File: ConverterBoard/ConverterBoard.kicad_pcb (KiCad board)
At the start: 2 copper layers, 60 x 55 mm, 51 parts, among them J1 PWR_IN, J2 PWR_OUT1, J3 PWR_OUT2, J4 PWR_OUT3, U1 RT6285, U2 RT6285, U3 RT6285

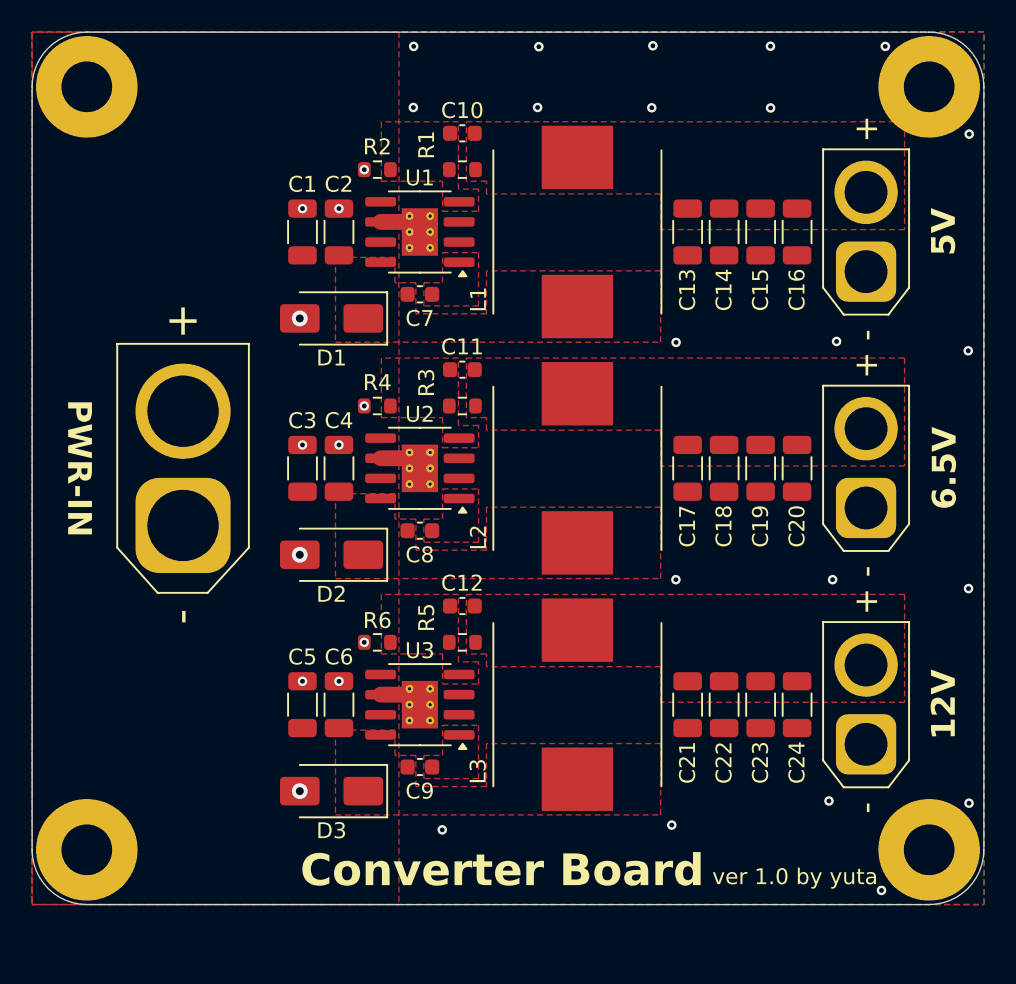
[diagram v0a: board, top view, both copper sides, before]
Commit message: Converter Board ver1.1
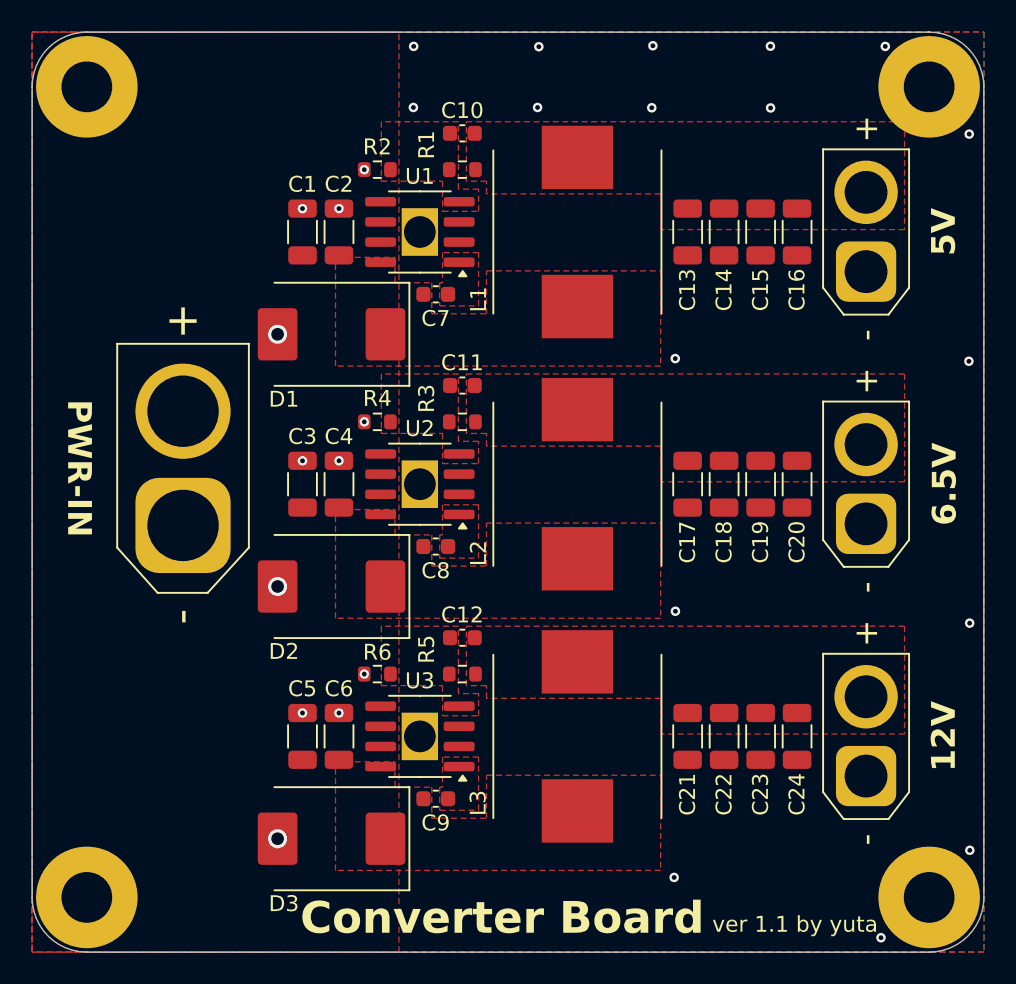
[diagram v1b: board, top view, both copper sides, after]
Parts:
- D1, D2, D3: footprint Diode_SMD:D_SMA -> Diode_SMD:D_SMC
- U1, U2, U3: footprint Package_SO:SOIC-8-1EP_3.9x4.9mm_P1.27mm_EP2.29x3mm_ThermalVias -> Anan-Robo_Footprint_Library:SOIC-8-1EP_3.9x4.9mm_P1.27mm_EP2.29x3mm_Handsoldering
- moved D3 3.00 mm to (122.8, 125.0)
- moved H6 3.00 mm to (121.0, 128.5)
- moved H3 3.00 mm to (107.3, 128.7)
- moved H4 3.00 mm to (160.4, 128.7)
- moved C9 2.24 mm to (129.3, 122.5)
- moved C12 2.00 mm to (131.0, 112.3)
- moved C21 2.00 mm to (145.2, 118.5)
- moved C22 2.00 mm to (147.5, 118.5)
- moved C23 2.00 mm to (149.8, 118.5)
- moved C24 2.00 mm to (152.1, 118.5)
- moved C5 2.00 mm to (120.9, 118.5)
- moved C6 2.00 mm to (123.2, 118.5)
- moved D2 2.00 mm to (122.8, 109.1)
- moved J4 2.00 mm to (156.4, 121.0)
- moved L3 2.00 mm to (138.2, 118.5)
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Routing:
- net GNDA: track 8.21 -> 0.90 mm, vias 33 -> 29
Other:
- board size 60 x 55 mm -> 60 x 58 mm
- board text added: "ver 1.1: 2025-06-12"
- board text removed: "ver 1.0: 2025-05-31"

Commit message: [Converter Board] : 基板上の日付を修正
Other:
- board text added: "ver 1.1: 2025-06-17"
- board text removed: "ver 1.1: 2025-06-12"
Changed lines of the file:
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@@
 		)
 	)
-	(gr_text "ver 1.1: 2025-06-12"
+	(gr_text "ver 1.1: 2025-06-17"
 		(at 136.5 76 180)
 		(layer "B.SilkS")
@@
 			(justify left mirror)
 		)
-		(render_cache "ver 1.1: 2025-06-12" 180
+		(render_cache "ver 1.1: 2025-06-17" 180
 			(polygon
 				(pts
@@
 			(polygon
 				(pts
-					(xy 154.829351 75.6791) (xy 154.834175 75.705449) (xy 154.849061 75.729878) (xy 154.960509 75.847921)
-					(xy 155.104783 76.002893) (xy 155.186775 76.092212) (xy 155.242536 76.154494) (xy 155.294926 76.220073)
-					(xy 155.33105 76.279131) (xy 155.351349 76.335355) (xy 155.358893 76.388967) (xy 155.352951 76.43921)
-					(xy 155.336193 76.479714) (xy 155.308848 76.512725) (xy 155.272983 76.536879) (xy 155.227215 76.552271)
-					(xy 155.16875 76.557861) (xy 155.098146 76.551505) (xy 155.022791 76.53163) (xy 154.940799 76.500415)
-					(xy 154.855582 76.456159) (xy 154.855582 76.682425) (xy 154.949005 76.71276) (xy 155.026088 76.731591)
-					(xy 155.110738 76.744001) (xy 155.190073 76.748004) (xy 155.27697 76.742566) (xy 155.357281 76.726682)
-					(xy 155.431396 76.698421) (xy 155.493349 76.657806) (xy 155.53984 76.610532) (xy 155.574462 76.553758)
-					(xy 155.595581 76.488456) (xy 155.603185 76.406993) (xy 155.597531 76.341872) (xy 155.580251 76.275834)
-					(xy 155.545188 76.205559) (xy 155.496646 76.134857) (xy 155.412163 76.041361) (xy 155.258876 75.883971)
-					(xy 155.164647 75.795457) (xy 155.10808 75.752812) (xy 155.065436 75.71515) (xy 155.606482 75.71515)
-					(xy 155.606482 75.502) (xy 154.829351 75.502)
-				)
-			)
+					(xy 155.355669 76.511919) (xy 154.845764 76.511919) (xy 154.845764 76.72507) (xy 155.619598 76.72507)
+					(xy 155.619598 76.554564) (xy 155.203189 75.502) (xy 154.957212 75.502)
+				)
+			)

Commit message: Converter Board ver1.2
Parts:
- added D4: BATT, LED_SMD:LED_0603_1608Metric, F.Cu at (107.0, 105.7)
- added D5: 5V, LED_SMD:LED_0603_1608Metric, F.Cu at (161.3, 85.6)
- added D6: 6.5V, LED_SMD:LED_0603_1608Metric, F.Cu at (161.3, 100.6)
- added D7: 12V, LED_SMD:LED_0603_1608Metric, F.Cu at (161.3, 116.8)
- added R10: 500, Resistor_SMD:R_0603_1608Metric, F.Cu at (161.3, 115.1)
- added R7: 1.5k, Resistor_SMD:R_0603_1608Metric, F.Cu at (107.0, 107.5)
- added R8: 240, Resistor_SMD:R_0603_1608Metric, F.Cu at (161.3, 83.8)
- added R9: 390, Resistor_SMD:R_0603_1608Metric, F.Cu at (161.3, 98.9)
- L3: value 33u -> 22u
- R6: value 11.3k -> 18k
- moved H7 7.50 mm to (142.0, 109.8)
- moved H8 7.50 mm to (142.2, 94.5)
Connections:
- net +12VA renamed +8VA
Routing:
- net +5VA: track 0.00 -> 4.60 mm
- net +8VA: track 0.00 -> 4.36 mm
- net +6.5VA: track 0.00 -> 4.24 mm
- net Net-(D7-K): track 0.00 -> 1.75 mm
- net Net-(D6-K): track 0.00 -> 1.75 mm
- net Net-(D5-K): track 0.00 -> 1.75 mm
- net Net-(D4-K): track 0.00 -> 1.75 mm
- net GNDA: vias 29 -> 30
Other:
- board text added: "8V"
- board text added: "ver 1.2: 2025-09-10"
- board text removed: "12V"
- board text removed: "ver 1.1: 2025-06-17"
